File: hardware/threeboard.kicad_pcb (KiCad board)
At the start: 2 copper layers, 58.2 x 50 mm, 51 parts, among them J1 USB_mini_micro_B, K1 KEYSW, K2 KEYSW, K3 KEYSW, SW1 SW_PUSH, U1 ATMEGA32U4, U2 24LC512, X1 XTAL_GND

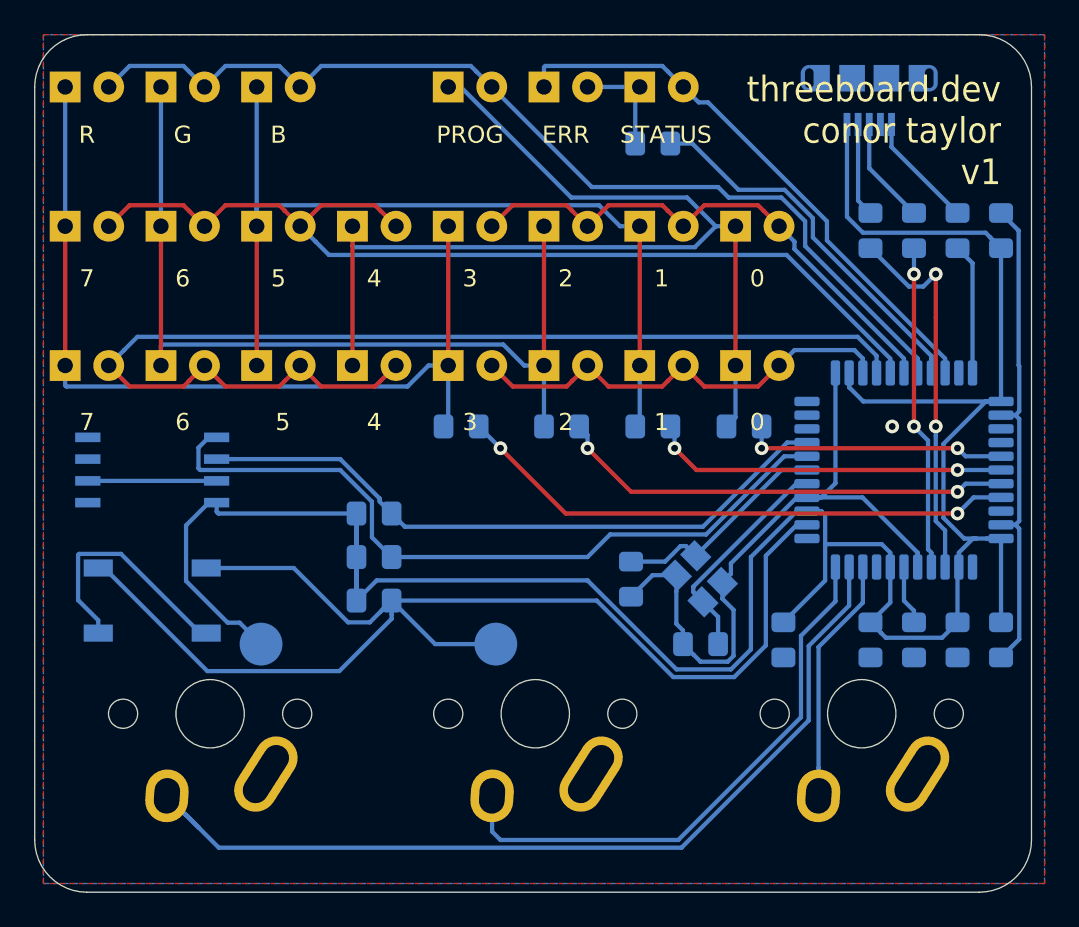
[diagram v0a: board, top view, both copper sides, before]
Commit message: Add v1 hardware revision with reinforced USB, better LED placement, and dual SMD EEPROM
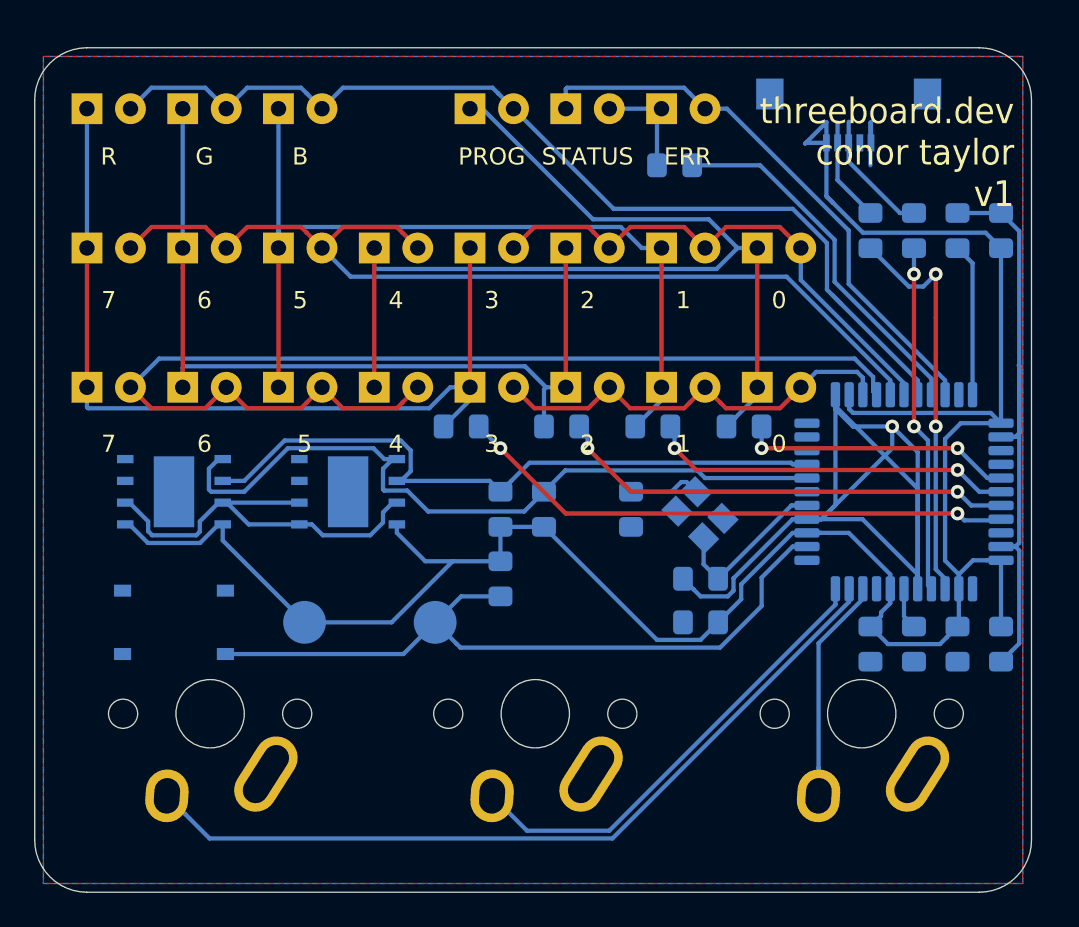
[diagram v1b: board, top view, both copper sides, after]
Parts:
- added U3: 24LC512, 24LC512-I_MF:DFN500X600X95-9N, B.Cu at (65.9, 51.9)
- J1: footprint 10118194-0001LF:AMPHENOL_10118194-0001LF -> USB3070-XX-X_REVE:GCT_USB3070-XX-X_REVE
- SW1: footprint Button_Switch_SMD:SW_SPST_TL3342 -> PTS526_SK08_SMTR2_LFS:SW_PTS526_SK08_SMTR2_LFS
- U2: footprint 24LC512:SOIC127P794X203-8N -> 24LC512-I_MF:DFN500X600X95-9N
- moved R10 10.3 mm to (77.3, 52.9), turned to 90 degrees
- moved R1 7.48 mm to (74.8, 57.0), turned to 270 degrees
- moved R11 7.38 mm to (74.8, 52.9), turned to 90 degrees
- moved C6 4.94 mm to (86.4, 59.5), turned to 180 degrees
- moved C2 4.07 mm to (82.4, 52.9)
- moved C1 3.81 mm to (86.4, 57.0)
- moved REF** 3.76 mm to (71.0, 59.5)
- moved X1 3.74 mm to (86.4, 53.3)
- moved REF** 2.84 mm to (63.3, 59.5)
- moved ERR 1.80 mm to (84.2, 29.6)
- moved PROG 1.80 mm to (73.0, 29.6)
- moved R9 1.80 mm to (84.9, 32.9)
- moved 1 1.80 mm to (84.2, 37.7)
- moved 1 1.80 mm to (84.2, 45.8)
- moved 3 1.80 mm to (73.0, 37.7)
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- renumbered STATUS to ERR, ERR to STATUS
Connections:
- U2 pad 1: GND -> VCC
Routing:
- net Net-(R1-Pad2): track 75.4 -> 43.2 mm
- net GND: track 97.3 -> 128.9 mm
- net VCC: track 145.1 -> 134.6 mm
- net /switch2: track 32.9 -> 27.3 mm
- net /switch1: track 52.8 -> 47.3 mm
- net Net-(C1-Pad1): track 13.1 -> 9.70 mm
- net Net-(C2-Pad1): track 12.9 -> 10.7 mm
- net /eeprom_scl: track 38.2 -> 39.8 mm
- net Net-(D21-Pad2): track 7.54 -> 6.09 mm
- net /row2: track 66.8 -> 65.4 mm
- net /row0: track 58.3 -> 57.0 mm
- net Net-(R2-Pad2): track 7.65 -> 8.92 mm
- net Net-(R4-Pad1): track 19.0 -> 20.3 mm
- net Net-(R3-Pad1): track 22.4 -> 23.6 mm
- net /switch3: track 14.4 -> 13.2 mm
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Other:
- board size 58.2 x 50 mm -> 58.2 x 49.3 mm
